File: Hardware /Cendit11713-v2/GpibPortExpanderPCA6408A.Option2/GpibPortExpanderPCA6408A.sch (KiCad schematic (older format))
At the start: 46 parts, among them P1 CONN_01X07, U1 PCA6408A, U2 PCA6408A

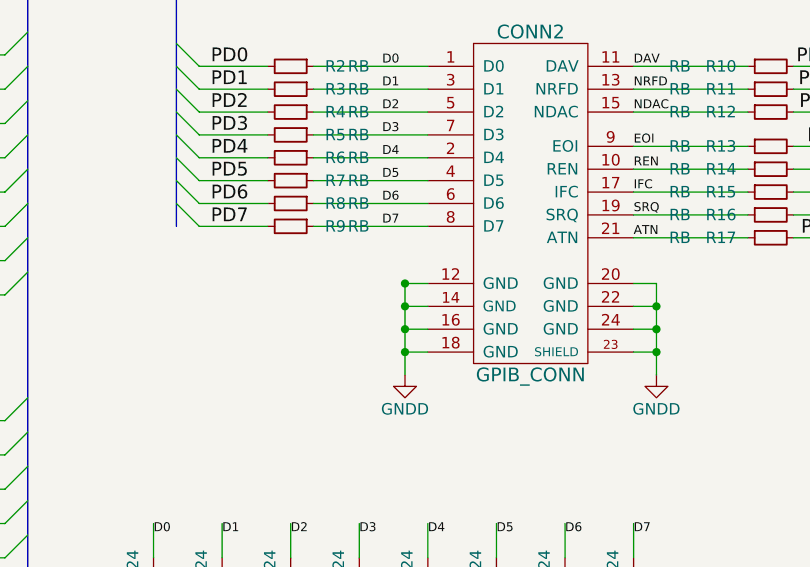
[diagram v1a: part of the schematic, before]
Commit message: En Cendit11713 + CenditLab respaldo
  - Se revisan tarjetas
  - Correccion en PCB GPIB
  - Se inicia tarjeta madre en una pieza (MainBoard.OnePiece)
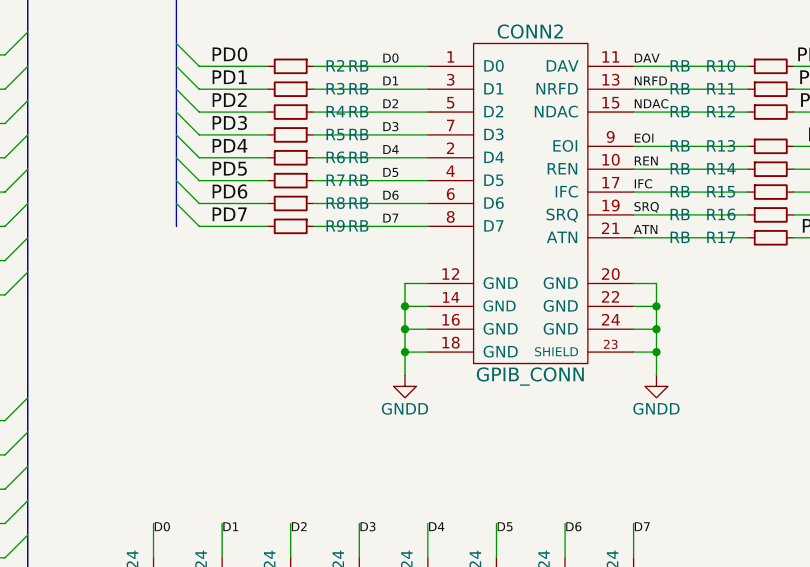
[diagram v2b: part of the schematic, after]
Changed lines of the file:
@@
 Wire Wire Line
 	6750 3050 6650 3050
-Connection ~ 6650 3050
 Wire Wire Line
 	1700 3550 1950 3550
